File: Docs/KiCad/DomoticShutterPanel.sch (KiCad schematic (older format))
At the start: 34 parts, among them J1 Conn_01x12, J10 Conn_01x03, J11 Conn_01x03, J12 Conn_01x03, J13 Conn_01x03, J14 Conn_01x03, J2 Conn_01x12, J3 Conn_01x06, J4 Conn_01x02, J5 Conn_01x02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

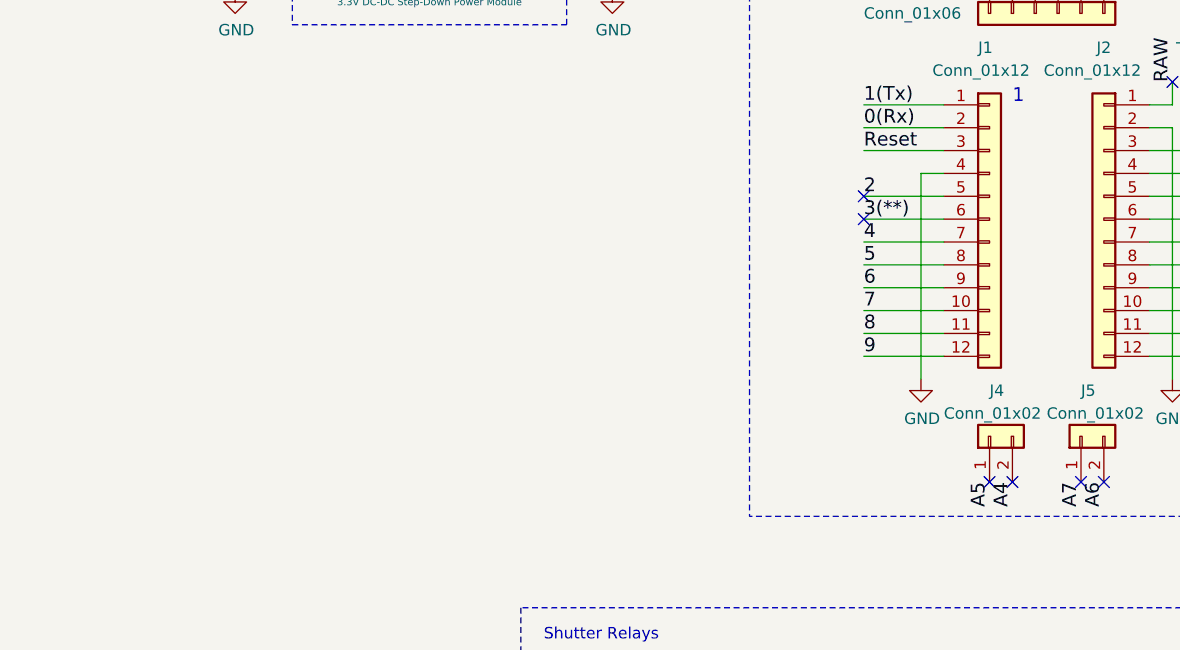
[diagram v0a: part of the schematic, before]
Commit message: 3V3 Power Module Library
Added ESP and LCD connectors to schematic
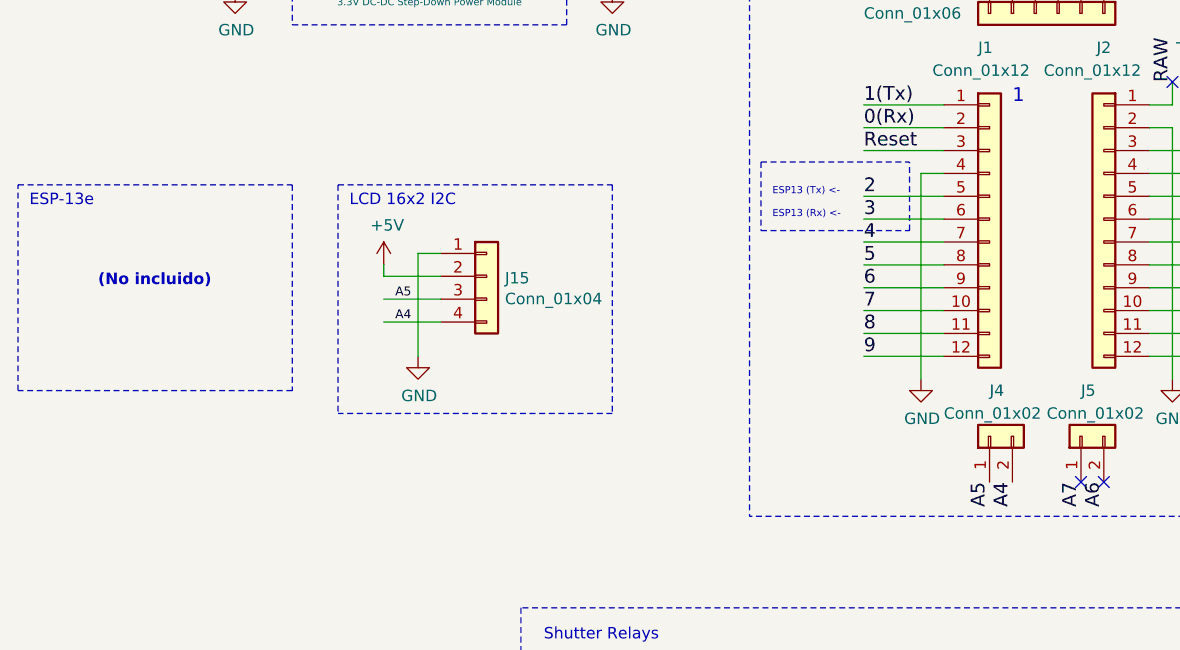
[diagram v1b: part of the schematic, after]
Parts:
- added J15: Conn_01x04, symbol CustomLibraries_connectors:Conn_01x04
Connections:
- net labels added: 3
- net labels removed: 3(**)
- wire segments 129 -> 135
- no-connect marks 12 -> 8
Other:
- note added: "(No incluido)"
- note added: "ESP-13e"
- note added: "ESP13 (Rx) <-"
- note added: "ESP13 (Tx) <-"
- note added: "LCD 16x2 I2C"
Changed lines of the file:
@@
 encoding utf-8
 Sheet 1 1
-Title ""
-Date "sam. 04 avril 2015"
+Title "Roller Shutter Controller Panel"
+Date "2020-04-21"
 Rev ""
 Comp ""
-Comment1 ""
+Comment1 "Relays approach"
 Comment2 ""
 Comment3 ""
@@
 2
 Text Label 4450 2250 0    60   ~ 0
-3(**)
+3
 Text Label 4450 2350 0    60   ~ 0
 4
@@
 NoConn ~ 5500 3400
 NoConn ~ 5400 3400
-NoConn ~ 5100 3400
-NoConn ~ 5000 3400
-NoConn ~ 4450 2150
-NoConn ~ 4450 2250
 NoConn ~ 5950 2150
 NoConn ~ 5950 2250
@@
 Wire Wire Line
 	3000 6950 2900 6950
+Wire Notes Line
+	1950 2100 1950 3000
+Wire Notes Line
+	750  3000 750  2100
+Text Notes 800  2200 0    50   ~ 0
+ESP-13e
+Text Notes 1100 2550 0    50   ~ 10
+(No incluido)
+Wire Notes Line
+	4000 2000 4000 2300
+Wire Notes Line
+	4650 2300 4650 2000
+Text Notes 4050 2150 0    31   ~ 0
+ESP13 (Tx) <-
+Text Notes 4050 2250 0    31   ~ 0
+ESP13 (Rx) <-
+Wire Notes Line
+	4000 2000 4650 2000
+Wire Notes Line
+	4000 2300 4650 2300
+Text Notes 2200 2200 0    50   ~ 0
+LCD 16x2 I2C
+$Comp
+L CustomLibraries_connectors:Conn_01x04 J15
+U 1 1 5EA32128
+P 2800 2500
+F 0 "J15" H 2880 2492 50  0000 L CNN
+F 1 "Conn_01x04" H 2880 2401 50  0000 L CNN
+F 2 "" H 2800 2500 50  0001 C CNN
+F 3 "~" H 2800 2500 50  0001 C CNN
+	1    2800 2500
+	1    0    0    -1
+$EndComp
+Wire Wire Line
+	2600 2400 2500 2400
+Wire Wire Line
+	2600 2500 2350 2500
+Wire Wire Line
+	2600 2600 2350 2600
+Wire Wire Line
+	2600 2700 2350 2700
+$Comp
+L CustomLibraries_power:GND #PWR08
+U 1 1 5EA49EAB
+P 2500 2850
+F 0 "#PWR08" H 2500 2600 50  0001 C CNN
+F 1 "GND" H 2505 2677 50  0000 C CNN
+F 2 "" H 2500 2850 50  0001 C CNN
+F 3 "" H 2500 2850 50  0001 C CNN
+	1    2500 2850
+	1    0    0    -1
+$EndComp
+Wire Wire Line
+	2500 2850 2500 2400
+Wire Wire Line
+	2350 2500 2350 2450
+$Comp
+L CustomLibraries_power:+5V #PWR04
+U 1 1 5EA685C8
+P 2350 2450
+F 0 "#PWR04" H 2350 2300 50  0001 C CNN
+F 1 "+5V" H 2365 2623 50  0000 C CNN
+F 2 "" H 2350 2450 50  0001 C CNN
+F 3 "" H 2350 2450 50  0001 C CNN
+	1    2350 2450
+	1    0    0    -1
+$EndComp
+Text Label 2400 2700 0    39   ~ 0
+A4
+Wire Notes Line
+	2150 2100 3350 2100
+Wire Notes Line
+	1950 3000 750  3000
+Wire Notes Line
+	750  2100 1950 2100
+Text Label 2400 2600 0    39   ~ 0
+A5
+Wire Notes Line
+	3350 3100 2150 3100
+Wire Notes Line
+	3350 2100 3350 3100
+Wire Notes Line
+	2150 2100 2150 3100
 $EndSCHEMATC

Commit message: Changed to radio approach
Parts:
- removed J1, J2: Conn_01x12, Custom_libraries:Socket_Strip_Arduino_1x12, symbol CustomLibraries_connectors:Conn_01x12
- removed J10, J11, J12, J13, J8, J9: Conn_01x03, Custom_libraries:ScrewTerminal_01X03_5mm, symbol CustomLibraries_connectors:Conn_01x03
- removed J3: Conn_01x06, Custom_libraries:Socket_Strip_Arduino_1x06, symbol CustomLibraries_connectors:Conn_01x06
- removed J5: Conn_01x02, Custom_libraries:Socket_Strip_Arduino_1x02, symbol CustomLibraries_connectors:Conn_01x02
- removed K1, K2, K3, K4, K5, K6: SRD-05VDC-SL-C, symbol CustomLibraries_SRD-05VDC-SL-C:SRD-05VDC-SL-C
- removed U1: ULN2803A, symbol CustomLibraries_ULN2803A:ULN2803A
- added C5, C6: 0.1uF, symbol CustomLibraries_Device:C
- added J5: UART COM, symbol CustomLibraries_connectors:Conn_01x03
- added J6: Conn_01x04, symbol CustomLibraries_connectors:Conn_01x04
- added J7: Conn_01x03, symbol CustomLibraries_connectors:Conn_01x03
- added R5, R6, R7, R8, R9: 10k, symbol CustomLibraries_Device:R
- added SW5: SW_Push, symbol CustomLibraries_Switch:SW_Push
- added U1: ESP-13-WROOM-02, Custom_libraries:ESP-13-WROOM-02, symbol ESP8266:ESP-13-WROOM-02
- added U2: Arduino_MiniPro, Custom_libraries:Socket_Strip_Arduino_MiniPro, symbol CustomLibraries_connectors:Arduino_MiniPro
- J4: value Conn_01x02 -> BOOT OPTION; footprint Custom_libraries:Socket_Strip_Arduino_1x02 -> (none)
- renumbered J6 to J1, J7 to J2, J15 to J3, J14 to J9, K7 to K1
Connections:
- net labels added: +3V3
- wire segments 135 -> 136
- no-connect marks 8 -> 24
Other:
- note added: "Radio modules"
- note removed: "(No incluido)"
- note removed: "Shutter Relays"
- moved on the sheet: C1, C2, C3, C4, J1, J2, J3, J9, K1, R1, R2, R3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

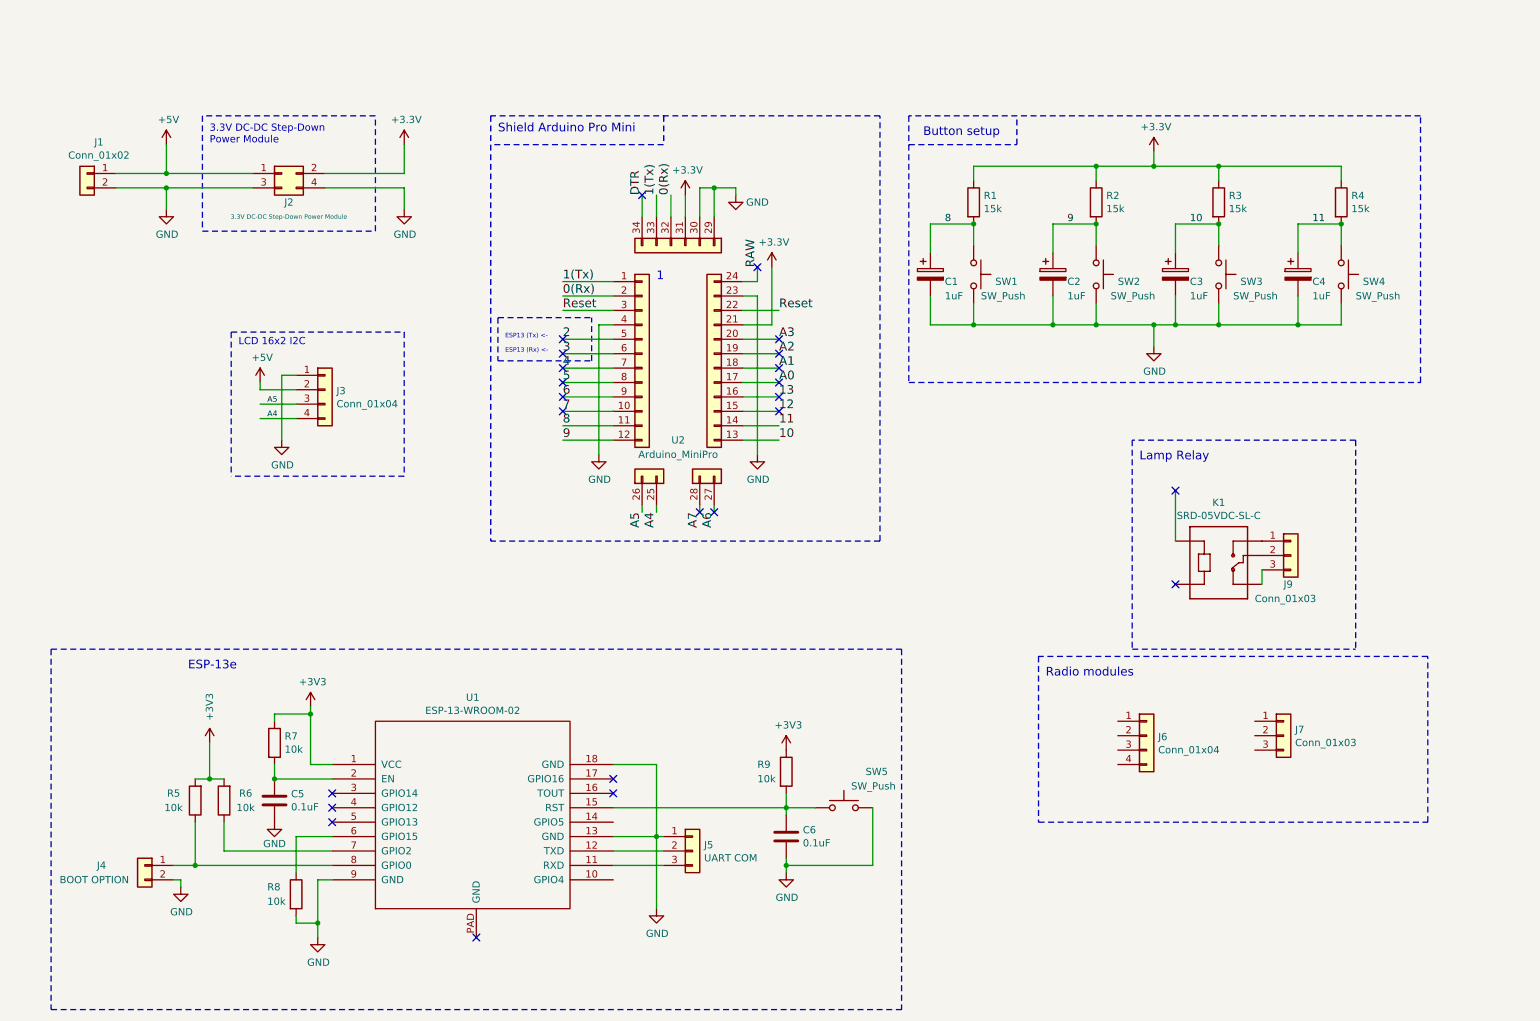
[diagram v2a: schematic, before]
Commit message: Changed architecture to ESP8266 as master
See documentation
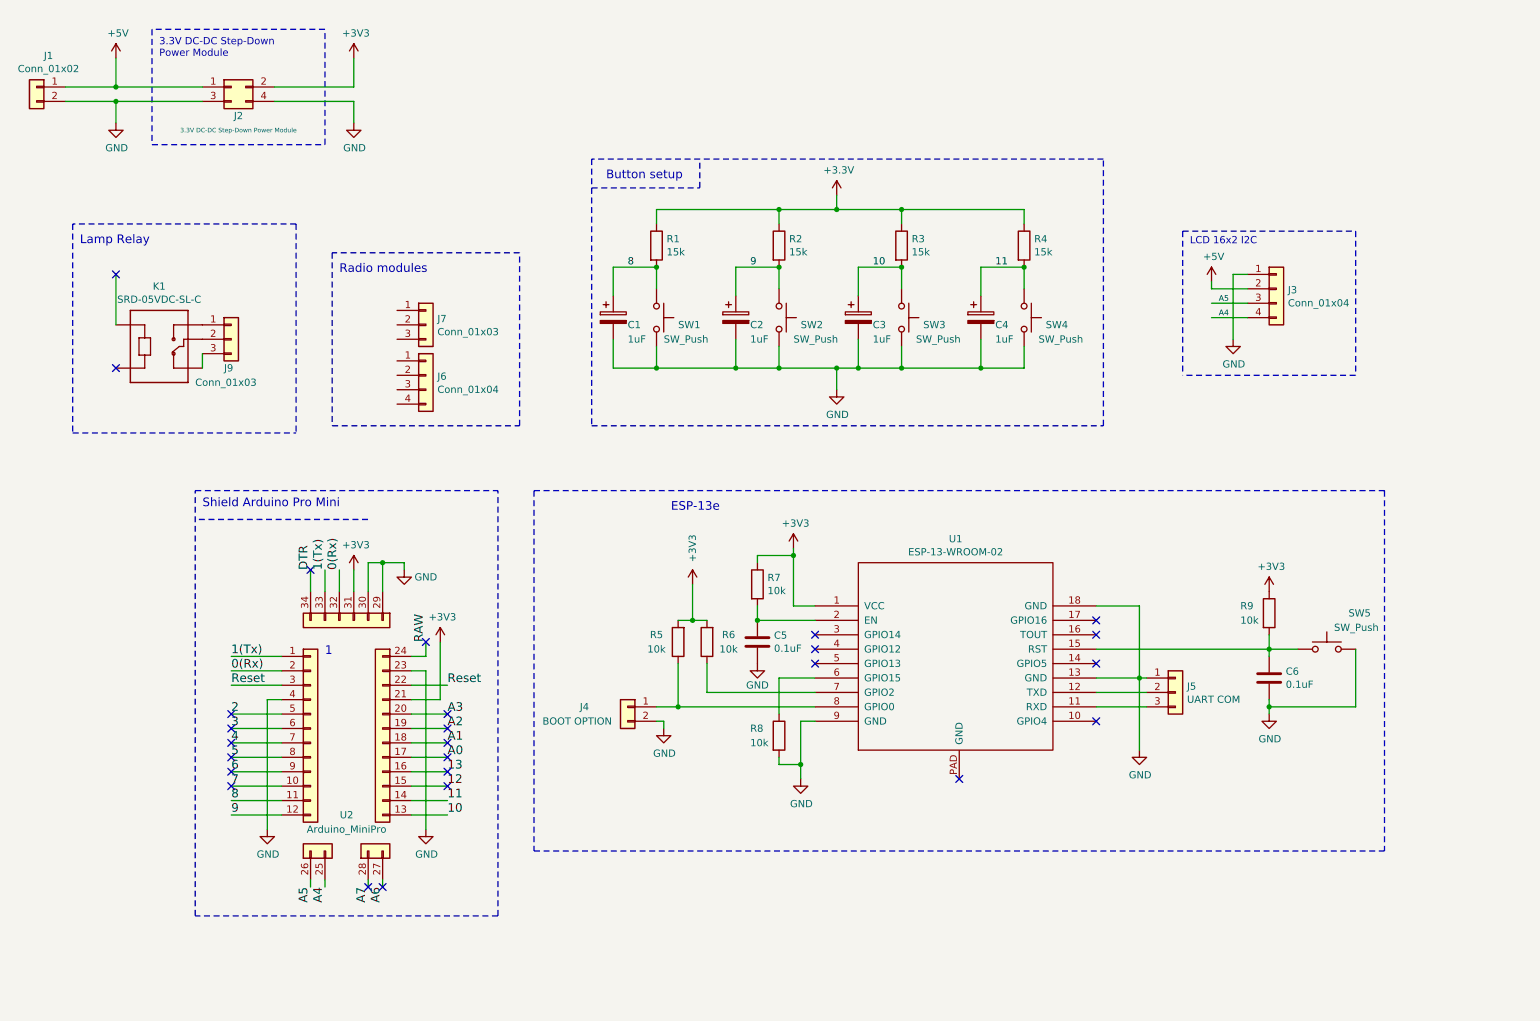
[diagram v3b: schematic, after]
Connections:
- no-connect marks 24 -> 26
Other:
- note removed: "ESP13 (Rx) <-"
- note removed: "ESP13 (Tx) <-"
- moved on the sheet: C1, C2, C3, C4, C5, C6, J1, J2, J3, J4, J5, J6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

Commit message: lcd stm Diagram
* lcd diagram nearly completed
* Added new 3d library for arduino pro mini
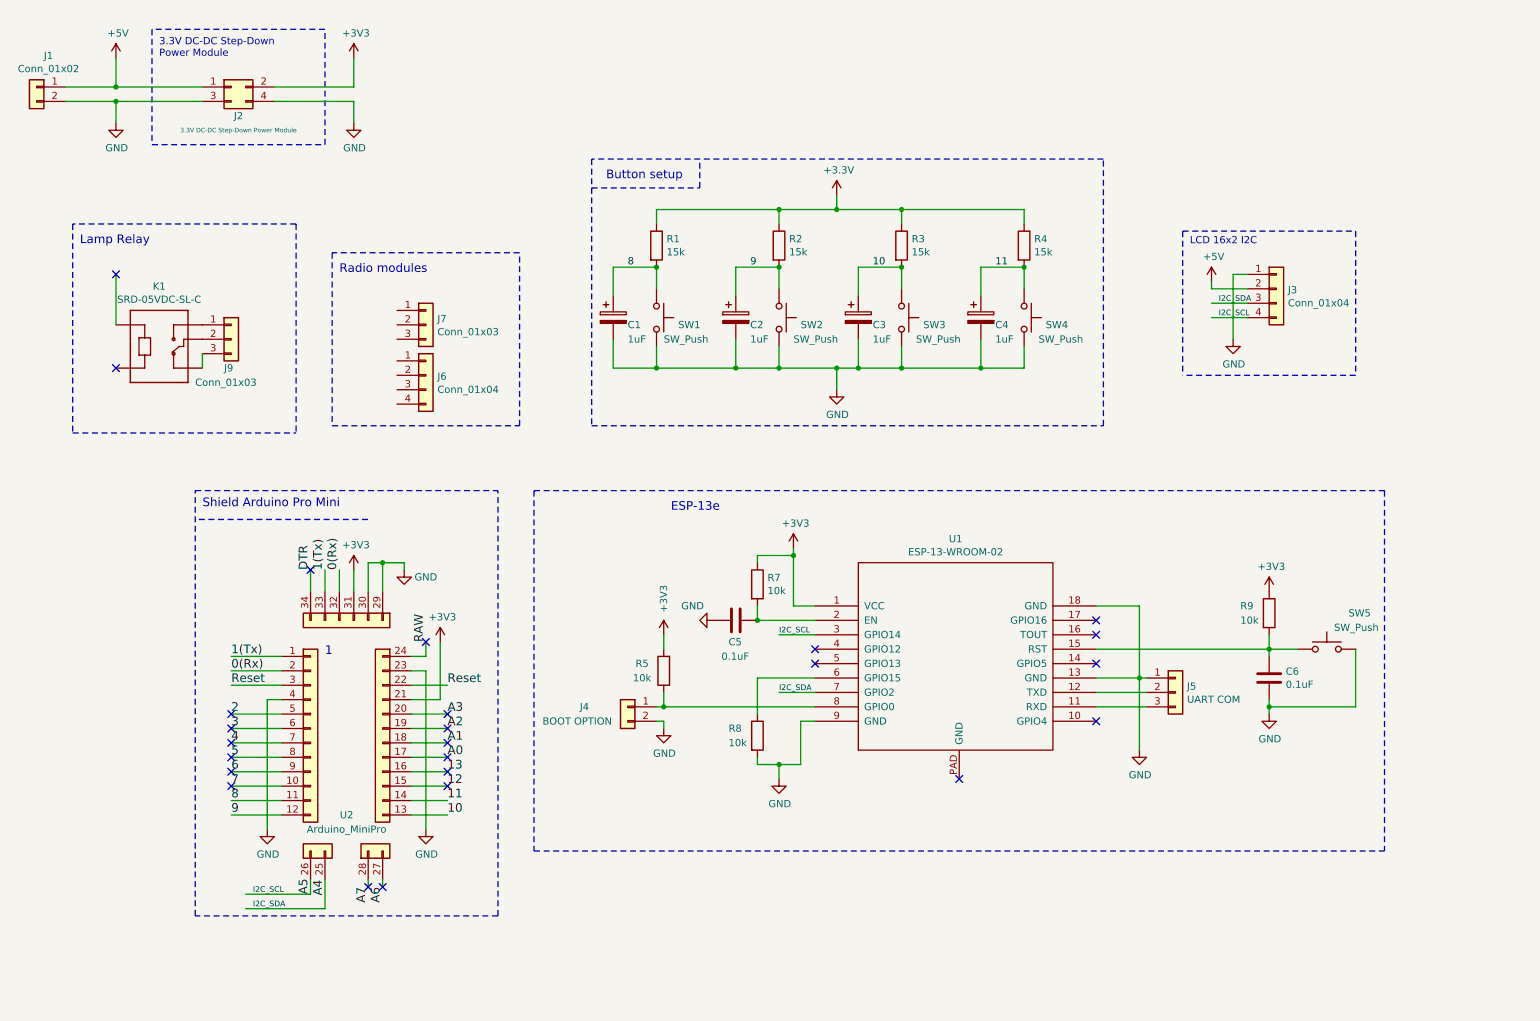
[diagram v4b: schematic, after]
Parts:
- removed R6: 10k, symbol CustomLibraries_Device:R
- C1, C2, C3, C4, C5, C6: footprint (none) -> Capacitor_THT:C_Radial_D5.0mm_H5.0mm_P2.00mm
- J1: footprint (none) -> Custom_libraries:PinSocket_1x02_P2.54mm_Vertical
- J2: footprint (none) -> Custom_libraries:DCDC_3v3_PowerModule
- J3, J6: footprint (none) -> Connector_PinHeader_2.54mm:PinHeader_1x04_P2.54mm_Vertical
- J4: footprint (none) -> Connector_PinHeader_2.54mm:PinHeader_1x02_P2.54mm_Vertical
- J5, J7: footprint (none) -> Connector_PinHeader_2.54mm:PinHeader_1x03_P2.54mm_Vertical
- J9: footprint Custom_libraries:ScrewTerminal_01X03_5mm -> Connector_PinHeader_2.54mm:PinHeader_1x03_P2.54mm_Vertical
- K1: footprint (none) -> Custom_libraries:RELAY_SRD-05VDC-SL-C
- R1, R2, R3, R4, R5, R7, R8, R9: footprint (none) -> Resistor_THT:R_Axial_DIN0204_L3.6mm_D1.6mm_P1.90mm_Vertical
- SW1, SW2, SW3, SW4, SW5: footprint (none) -> Custom_libraries:SW_PUSH_6mm
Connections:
- net A4: now also J3.3 (Pin_3), U1.7 (GPIO2); no longer J3.4 (Pin_4)
- net A5: now also J3.4 (Pin_4), U1.3 (GPIO14); no longer J3.3 (Pin_3)
- no-connect marks 26 -> 25
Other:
- moved on the sheet: C5, R5, R8

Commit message: EEPROM storing and UI completed
Also a sketch in Processing was developed to test the UCD principles for the UI.
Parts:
- added J?: Conn_01x03, Connector_PinHeader_2.54mm:PinHeader_1x03_P2.54mm_Vertical, symbol CustomLibraries_connectors:Conn_01x03
- added J?: Conn_01x02, symbol CustomLibraries_connectors:Conn_01x02
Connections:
- net labels added: GPIO12, GPIO13, GPIO4, GPIO5
- wire segments 137 -> 144
- no-connect marks 25 -> 18
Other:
- note added: "Lamp button"
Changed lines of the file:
@@
 	7600 1950 7600 2050
 Connection ~ 6750 1950
-Text Label 4850 2350 0    50   ~ 0
-8
-Text Label 5700 2350 0    50   ~ 0
-9
-Text Label 6550 2350 0    50   ~ 0
-10
-Text Label 7400 2350 0    50   ~ 0
-11
 Wire Notes Line
 	4600 1600 4600 3450
@@
 Wire Wire Line
 	950  1100 1300 1100
-NoConn ~ 8100 5500
-NoConn ~ 8100 5100
 Wire Notes Line
 	4200 3900 10100 3900
 Wire Wire Line
-	8100 5000 9300 5000
+	8100 5000 8850 5000
 Connection ~ 9300 5000
 Wire Wire Line
@@
 	1    0    0    -1
 $EndComp
-NoConn ~ 6150 5100
-NoConn ~ 6150 5000
 $Comp
 L CustomLibraries_power:GND #PWR014
@@
 Wire Notes Line
 	3950 6850 3950 3900
-NoConn ~ 2100 5450
-NoConn ~ 2100 5550
 NoConn ~ 2100 5650
-NoConn ~ 2100 5750
 NoConn ~ 2100 5850
 NoConn ~ 2100 5950
@@
 Text Label 2250 6800 0    39   ~ 0
 I2C_SDA
+$Comp
+L CustomLibraries_connectors:Conn_01x03 J?
+U 1 1 5F3D7AAB
+P 9250 1100
+F 0 "J?" H 9330 1142 50  0000 L CNN
+F 1 "Conn_01x03" H 9330 1051 50  0000 L CNN
+F 2 "Connector_PinHeader_2.54mm:PinHeader_1x03_P2.54mm_Vertical" H 9250 1100 50  0001 C CNN
+F 3 "~" H 9250 1100 50  0001 C CNN
+	1    9250 1100
+	1    0    0    -1
+$EndComp
+Wire Notes Line
+	8750 1550 9900 1550
+Wire Notes Line
+	9900 1550 9900 600
+Wire Notes Line
+	9900 600  8750 600
+Wire Notes Line
+	8750 600  8750 1550
+Text Notes 8800 700  0    39   ~ 0
+Lamp button
+Wire Wire Line
+	6150 5000 5900 5000
+Wire Wire Line
+	6150 5100 5900 5100
+Wire Wire Line
+	8100 5500 8350 5500
+Wire Wire Line
+	8100 5100 8350 5100
+Text Label 5900 5000 0    39   ~ 0
+GPIO12
+Text Label 5900 5100 0    39   ~ 0
+GPIO13
+Text Label 8150 5500 0    39   ~ 0
+GPIO4
+Text Label 8150 5100 0    39   ~ 0
+GPIO5
+Text Label 4750 2350 0    39   ~ 0
+GPIO4
+Text Label 5600 2350 0    39   ~ 0
+GPIO5
+Text Label 6450 2350 0    39   ~ 0
+GPIO12
+Text Label 7300 2350 0    39   ~ 0
+GPIO13
+$Comp
+L CustomLibraries_connectors:Conn_01x02 J?
+U 1 1 5F401437
+P 8650 4700
+F 0 "J?" H 8600 4400 50  0000 C CNN
+F 1 "Conn_01x02" H 8800 4500 50  0000 C CNN
+F 2 "" H 8650 4700 50  0001 C CNN
+F 3 "~" H 8650 4700 50  0001 C CNN
+	1    8650 4700
+	-1   0    0    1
+$EndComp
+Wire Wire Line
+	8850 4700 8850 5000
+Connection ~ 8850 5000
+Wire Wire Line
+	8850 5000 9300 5000
+Text Label 8850 4550 0    39   ~ 0
+Reset
+Wire Wire Line
+	8850 4600 8850 4500
 $EndSCHEMATC
